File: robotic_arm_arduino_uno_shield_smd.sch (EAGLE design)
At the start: 39 parts, among them J1 (ID,OD)=(2.1,5.5)MM

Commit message: Adjusted some of the traces
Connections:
- net 5V: now also PLAY_SW.3, REC_SW.1; no longer PLAY_SW.1, REC_SW.3
- net D7: now also REC_SW.3; no longer REC_SW.1
- net D8: now also PLAY_SW.1; no longer PLAY_SW.3
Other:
- moved on the sheet: PLAY_SW, REC_SW
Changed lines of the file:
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@@
 <setting verticaltext="up"/>
 </settings>
-<grid distance="0.1" unitdist="inch" unit="inch" style="lines" multiple="1" display="no" altdistance="0.01" altunitdist="inch" altunit="inch"/>
+<grid distance="0.1" unitdist="inch" unit="inch" style="lines" multiple="1" display="yes" altdistance="0.01" altunitdist="inch" altunit="inch"/>
 <layers>
 <layer number="1" name="Top" color="4" fill="1" visible="no" active="no"/>
@@
 <instance part="SUPPLY5" gate="G$2" x="220.98" y="22.86"/>
 <instance part="SUPPLY6" gate="G$1" x="281.94" y="22.86"/>
-<instance part="REC_SW" gate="G$1" x="297.18" y="91.44" rot="R90"/>
-<instance part="PLAY_SW" gate="G$1" x="327.66" y="91.44" rot="R270"/>
+<instance part="REC_SW" gate="G$1" x="297.18" y="91.44" rot="R270"/>
+<instance part="PLAY_SW" gate="G$1" x="327.66" y="91.44" rot="R90"/>
 <instance part="R2" gate="G$1" x="327.66" y="73.66" rot="R90"/>
 <instance part="GND7" gate="GND" x="297.18" y="60.96"/>
@@
 <wire x1="335.28" y1="81.28" x2="327.66" y2="81.28" width="0.1524" layer="91"/>
 <label x="335.28" y="81.28" size="1.27" layer="95" ratio="10" xref="yes"/>
-<pinref part="PLAY_SW" gate="G$1" pin="3"/>
+<pinref part="PLAY_SW" gate="G$1" pin="1"/>
 <wire x1="327.66" y1="86.36" x2="327.66" y2="81.28" width="0.1524" layer="91"/>
 <junction x="327.66" y="81.28"/>
@@
 <segment>
 <pinref part="R1" gate="G$1" pin="2"/>
-<pinref part="REC_SW" gate="G$1" pin="1"/>
 <wire x1="297.18" y1="78.74" x2="297.18" y2="81.28" width="0.1524" layer="91"/>
+<wire x1="297.18" y1="81.28" x2="304.8" y2="81.28" width="0.1524" layer="91"/>
+<label x="304.8" y="81.28" size="1.27" layer="95" ratio="10" xref="yes"/>
+<pinref part="REC_SW" gate="G$1" pin="3"/>
 <wire x1="297.18" y1="81.28" x2="297.18" y2="86.36" width="0.1524" layer="91"/>
-<wire x1="297.18" y1="81.28" x2="304.8" y2="81.28" width="0.1524" layer="91"/>
 <junction x="297.18" y="81.28"/>
-<label x="304.8" y="81.28" size="1.27" layer="95" ratio="10" xref="yes"/>
 </segment>
 </net>
@@
 <net name="5V" class="0">
 <segment>
-<pinref part="REC_SW" gate="G$1" pin="3"/>
-<wire x1="297.18" y1="96.52" x2="297.18" y2="101.6" width="0.1524" layer="91"/>
-<pinref part="SUPPLY8" gate="5V" pin="5V"/>
-</segment>
-<segment>
 <wire x1="180.34" y1="-30.48" x2="190.5" y2="-30.48" width="0.1524" layer="91"/>
 <wire x1="190.5" y1="-30.48" x2="190.5" y2="-25.4" width="0.1524" layer="91"/>
@@
 </segment>
 <segment>
-<pinref part="PLAY_SW" gate="G$1" pin="1"/>
-<pinref part="SUPPLY9" gate="5V" pin="5V"/>
-<wire x1="327.66" y1="96.52" x2="327.66" y2="101.6" width="0.1524" layer="91"/>
-</segment>
-<segment>
 <pinref part="SUPPLY15" gate="5V" pin="5V"/>
 <wire x1="215.9" y1="99.06" x2="215.9" y2="91.44" width="0.1524" layer="91"/>
@@
 <wire x1="215.9" y1="91.44" x2="200.66" y2="91.44" width="0.1524" layer="91"/>
 </segment>
-</net>
+<segment>
+<pinref part="SUPPLY9" gate="5V" pin="5V"/>
+<pinref part="PLAY_SW" gate="G$1" pin="3"/>
+<wire x1="327.66" y1="101.6" x2="327.66" y2="96.52" width="0.1524" layer="91"/>
+</segment>
+<segment>
+<pinref part="REC_SW" gate="G$1" pin="1"/>
+<pinref part="SUPPLY8" gate="5V" pin="5V"/>
+<wire x1="297.18" y1="96.52" x2="297.18" y2="101.6" width="0.1524" layer="91"/>
+</segment>
+</net>

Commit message: Adjusted some of the traces
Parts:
- removed R5: 10KΩ, MrSwirlyEyes:RESISTORSMD-0805_1/8W_10K_5%
- added R0: 10KΩ, MrSwirlyEyes:RESISTORSMD-0805_1/8W_10K_5%
- BATT1, BATT2: value (none) -> 6V
- POT1, POT2, POT3, POT4: value (none) -> 22K
- renumbered C7 to C6, D1 to PWR_LED, S0 to PWR_SW
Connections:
- net GND: now also R0.1; no longer R5.1
- net N$1: now also R4.2; no longer R5.2
- net N$2: now also R3.2; no longer R4.2
- net N$4: now also R0.2; no longer R3.2
- net VCC_1: now also D5.A; no longer D4.A
- net VCC_2: now also D4.A; no longer D5.A
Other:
- moved on the sheet: R3, R4

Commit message: Final version.  Sending to fab
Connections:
- net N$3 renamed VBATT
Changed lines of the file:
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@@
 </segment>
 </net>
-<net name="N$3" class="0">
+<net name="VBATT" class="0">
 <segment>
 <wire x1="187.96" y1="175.26" x2="177.8" y2="175.26" width="0.1524" layer="91"/>

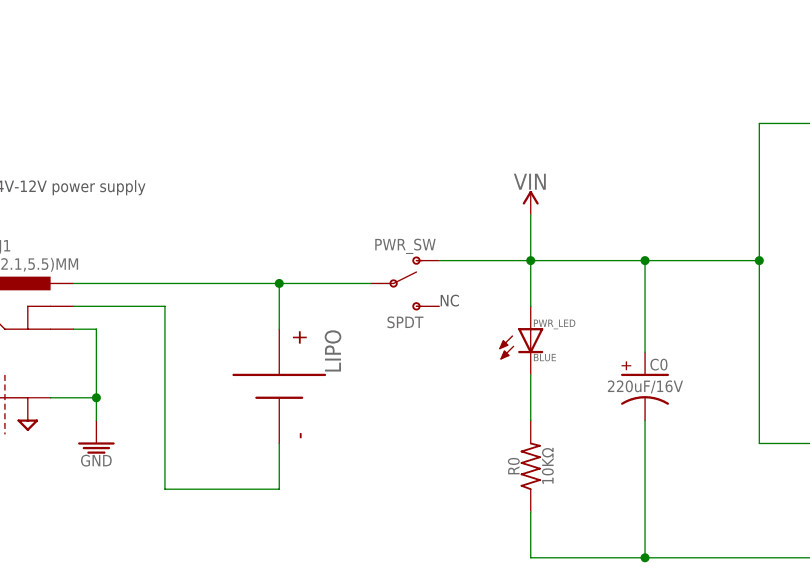
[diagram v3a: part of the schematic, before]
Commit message: Changed out switch.  Adjusted traces accordingly
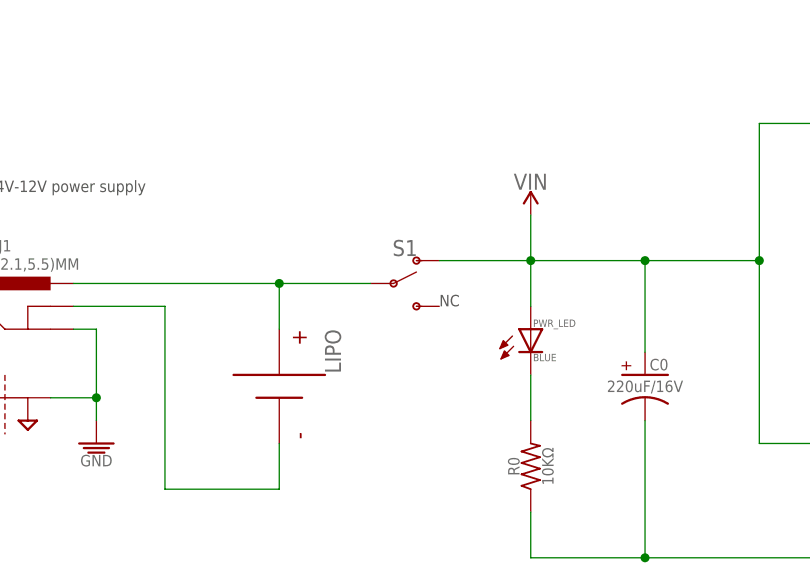
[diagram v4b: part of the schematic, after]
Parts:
- removed PWR_SW: SPDT, MrSwirlyEyes:SW_SPDT_RA_3A/28V/120VAC
- added S1: (no value), SparkFun-Switches:SWITCH-SPDT-PTH-11.6X4.0MM
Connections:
- net VBATT: now also S1.P; no longer PWR_SW.P
- net VIN: now also S1.O; no longer PWR_SW.S1
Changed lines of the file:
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@@
 <part name="C6" library="MrSwirlyEyes" deviceset="CAPACITOR_POLARIZED" device="_ALUM-ELECTROLYTIC_SMD_100UF-16V-20%" value="100UF/16V"/>
 <part name="LIPO" library="MrSwirlyEyes" deviceset="BATTERY" device=""/>
-<part name="PWR_SW" library="MrSwirlyEyes" deviceset="SW_SPDT_RA_3A/28V/120VAC" device="" value="SPDT"/>
 <part name="VREG1" library="MrSwirlyEyes" deviceset="VREG_LM340_LDO_1.5A-5V" device="" value="1.5A/5V"/>
 <part name="D4" library="MrSwirlyEyes" deviceset="DIODE_SMD_GP_1A-50V-SOD123F" device="" value="1A/50V"/>
@@
 <part name="NGND4" library="MrSwirlyEyes" deviceset="NGND" device=""/>
 <part name="NGND5" library="MrSwirlyEyes" deviceset="NGND" device=""/>
+<part name="S1" library="SparkFun-Switches" deviceset="SWITCH-SPDT" device="-PTH-11.6X4.0MM"/>
 </parts>
 <sheets>
@@
 <instance part="C6" gate="G$1" x="302.26" y="152.4"/>
 <instance part="LIPO" gate="G$1" x="177.8" y="162.56" rot="R270"/>
-<instance part="PWR_SW" gate="G$1" x="190.5" y="175.26"/>
 <instance part="VREG1" gate="G$1" x="264.16" y="193.04"/>
 <instance part="D4" gate="G$1" x="265.43" y="167.64" rot="R180"/>
@@
 <instance part="NGND4" gate="G$1" x="251.46" y="7.62"/>
 <instance part="NGND5" gate="G$1" x="281.94" y="7.62"/>
+<instance part="S1" gate="1" x="190.5" y="175.26"/>
 </instances>
 <busses>
@@
 <pinref part="PWR_LED" gate="G$1" pin="A"/>
 <wire x1="205.74" y1="172.72" x2="205.74" y2="177.8" width="0.1524" layer="91"/>
-<pinref part="PWR_SW" gate="G$1" pin="S1"/>
 <pinref part="VREG1" gate="G$1" pin="VI"/>
 <wire x1="254" y1="193.04" x2="251.46" y2="193.04" width="0.1524" layer="91"/>
@@
 <pinref part="D5" gate="G$1" pin="K"/>
 <wire x1="260.35" y1="203.2" x2="251.46" y2="203.2" width="0.1524" layer="91"/>
+<pinref part="S1" gate="1" pin="O"/>
 </segment>
 </net>
@@
 <junction x="177.8" y="175.26"/>
 <pinref part="LIPO" gate="G$1" pin="P"/>
-<pinref part="PWR_SW" gate="G$1" pin="P"/>
 <pinref part="J1" gate="G$1" pin="PWR"/>
-</segment>
-</net>
+<pinref part="S1" gate="1" pin="P"/>
+</segment>
+</net>

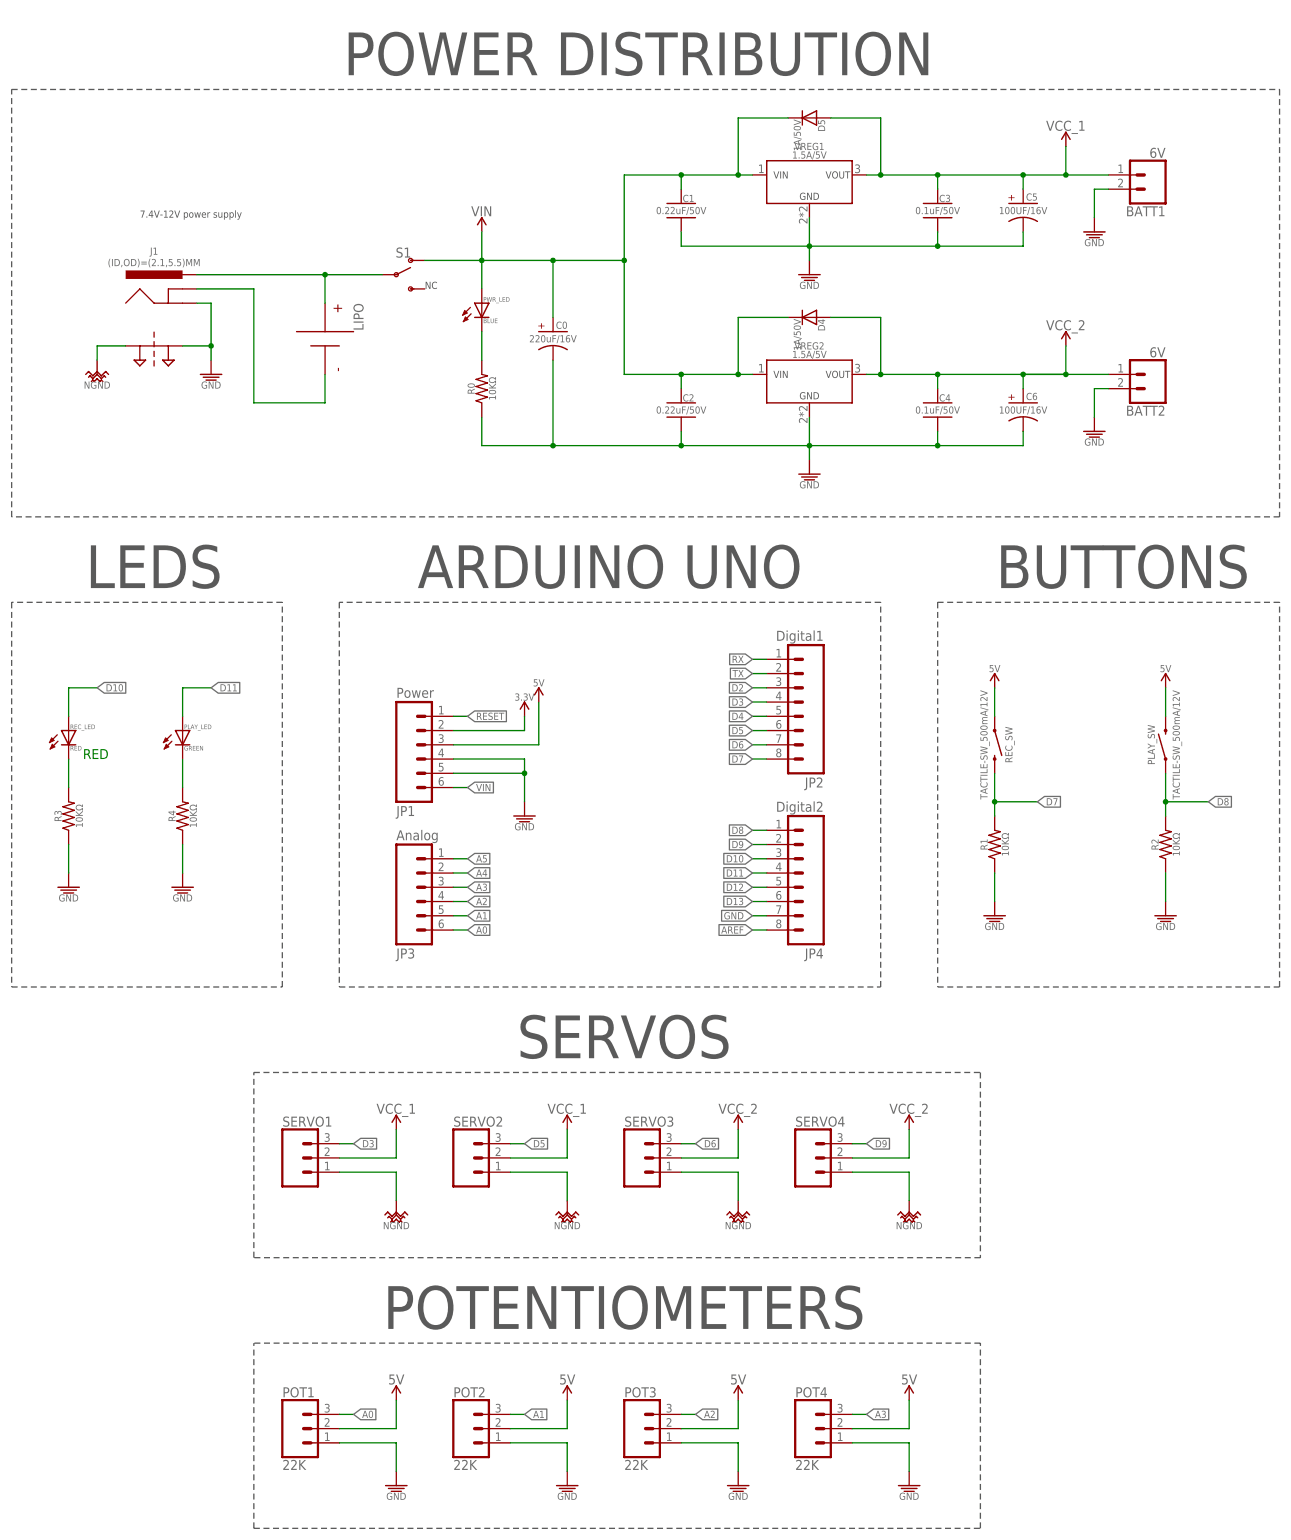
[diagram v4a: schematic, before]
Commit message: Rev 2.  Changed pad sizes of 805 SMD components.
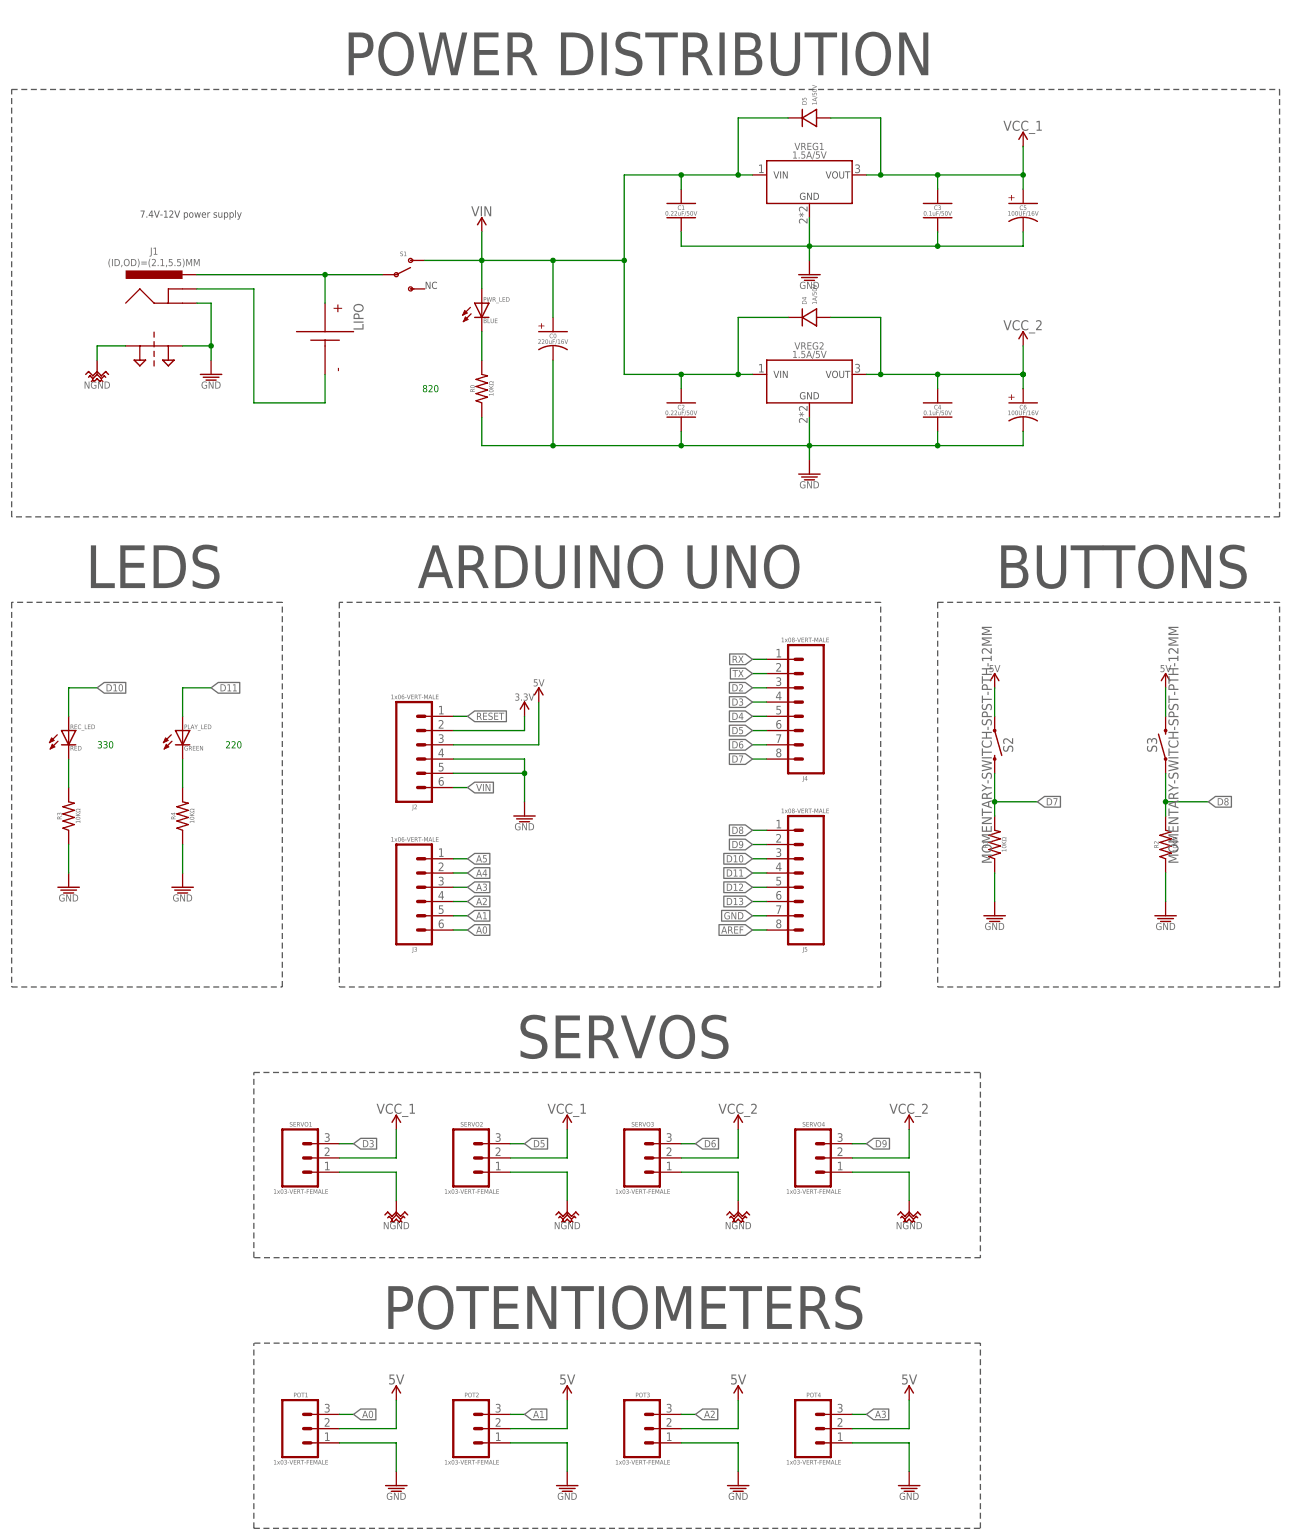
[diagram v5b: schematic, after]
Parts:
- removed BATT1, BATT2: 6V, SparkFun-Connectors:CONN_02
- removed JP1: Power, SparkFun:M06SIP
- removed JP2: Digital1, SparkFun:M08
- removed JP3: Analog, SparkFun:M06SIP
- removed JP4: Digital2, SparkFun:M08
- removed PLAY_SW, REC_SW: TACTILE-SW_500mA/12V, MrSwirlyEyes:SWITCH_MOMENTARY_SPST-NO_SMD_12V_50MA_5.2MM
- added J2, J3: 1x06-VERT-MALE, connectors:1X06VERT-MALE
- added J4, J5: 1x08-VERT-MALE, connectors:1X08VERT-MALE
- added S2, S3: MOMENTARY-SWITCH-SPST-PTH-12MM, SparkFun-Switches:MOMENTARY-SWITCH-SPST-PTH-12MM
- C0: device MrSwirlyEyes:CAPACITOR_POLARIZED_ALUM-ELECTROLYTIC_SMD_220UF-16V-20% -> MrSwirlyEyes:CAP_POLARIZED_ALUM-ELECTROLYTIC_SMD_220UF-16V-20%
- C1, C2: device MrSwirlyEyes:CAPACITOR_CERAMIC_SMD-805_0.22UF-50V-10% -> MrSwirlyEyes:CAP_CERAMIC_SMD-805_0.22UF-50V-10%
- C3, C4: device MrSwirlyEyes:CAPACITOR_CERAMIC_SMD-805_0.1UF-50V-10% -> MrSwirlyEyes:CAP_CERAMIC_SMD-805_0.1UF-50V-10%
- C5, C6: device MrSwirlyEyes:CAPACITOR_POLARIZED_ALUM-ELECTROLYTIC_SMD_100UF-16V-20% -> MrSwirlyEyes:CAP_POLARIZED_ALUM-ELECTROLYTIC_SMD_100UF-16V-20%
- D4, D5: device MrSwirlyEyes:DIODE_SMD_GP_1A-50V-SOD123F -> MrSwirlyEyes:DIODE_GEN-PURPSMD_GP_1A-50V-SOD123F
- LIPO: value BATTERY -> BATTERYPTH_HOLES; device MrSwirlyEyes:BATTERY -> MrSwirlyEyes:BATTERYPTH_HOLES
- PLAY_LED: device MrSwirlyEyes:LED-DISCRETE_SMD-805GREEN -> MrSwirlyEyes:LED_SMD-805_DISCRETE_GREEN
- POT1, POT2, POT3, POT4: value 22K -> 1x03-VERT-FEMALE; device SparkFun-Connectors:CONN_03 -> connectors:1X03VERT-FEMALE
- PWR_LED: device MrSwirlyEyes:LED-DISCRETE_SMD-805BLUE -> MrSwirlyEyes:LED_SMD-805_DISCRETE_BLUE
- REC_LED: device MrSwirlyEyes:LED-DISCRETE_SMD-805RED -> MrSwirlyEyes:LED_SMD-805_DISCRETE_RED
- S1: device SparkFun-Switches:SWITCH-SPDT-PTH-11.6X4.0MM -> MrSwirlyEyes:SWITCH_SPDT_SLIDE_RA_SMD_4V_300MA5A-28V_13L-7W
- SERVO1, SERVO2, SERVO3, SERVO4: value (none) -> 1x03-VERT-FEMALE; device SparkFun-Connectors:CONN_03 -> connectors:1X03VERT-FEMALE
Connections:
- net N$6 renamed -
- net VBATT renamed +
- net 3.3V: now also J2.2; no longer JP1.2
- net 5V: now also J2.3, S2.1, S3.2; no longer JP1.3, PLAY_SW.3, REC_SW.1
- net A0: now also J3.6; no longer JP3.6
- net A1: now also J3.5; no longer JP3.5
- net A2: now also J3.4; no longer JP3.4
- net A3: now also J3.3; no longer JP3.3
- net A4: now also J3.2; no longer JP3.2
- net A5: now also J3.1; no longer JP3.1
- net AREF: now also J5.8; no longer JP4.8
- net D10: now also J5.3; no longer JP4.3
- net D11: now also J5.4; no longer JP4.4
- net D12: now also J5.5; no longer JP4.5
- net D13: now also J5.6; no longer JP4.6
- net D2: now also J4.3; no longer JP2.3
- net D3: now also J4.4; no longer JP2.4
- net D4: now also J4.5; no longer JP2.5
- net D5: now also J4.6; no longer JP2.6
- net D6: now also J4.7; no longer JP2.7
- net D7: now also J4.8, S2.2; no longer JP2.8, REC_SW.3
- net D8: now also J5.1, S3.1; no longer JP4.1, PLAY_SW.1
- net D9: now also J5.2; no longer JP4.2
- net GND: now also J2.4, J2.5, J5.7; no longer BATT1.2, BATT2.2, JP1.4, JP1.5, JP4.7
- net RESET: now also J2.1; no longer JP1.1
- net RX: now also J4.1; no longer JP2.1
- net TX: now also J4.2; no longer JP2.2
- net VCC_1: no longer BATT1.1
- net VCC_2: no longer BATT2.1
- net VIN: now also J2.6, S1.S1; no longer JP1.6, S1.O
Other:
- note added: "220"
- note added: "330"
- note added: "820"
- note removed: "RED"

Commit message: Added switch object parameters for power switch and PLAY,RECORD buttons.  Added potentiometer from digikey to POT object.  Added Servo from Amazon to SERVO object MG90S
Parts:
- POT1, POT2, POT3, POT4: value 1x03-VERT-FEMALE -> 20KΩ; device connectors:1X03VERT-FEMALE -> MrSwirlyEyes:POTENTIOMETERNO-MARKINGS_VERT-FEMALE
- R3: value 10KΩ -> 2KΩ; device MrSwirlyEyes:RESISTORSMD-0805_1/8W_10K_5% -> MrSwirlyEyes:RESISTORSMD-0805_1/8W_2K_5%
- R4: value 10KΩ -> 1KΩ; device MrSwirlyEyes:RESISTORSMD-0805_1/8W_10K_5% -> MrSwirlyEyes:RESISTORSMD-0805_1/8W_1K_5%
- S1: value (none) -> 5A/28V; device MrSwirlyEyes:SWITCH_SPDT_SLIDE_RA_SMD_4V_300MA5A-28V_13L-7W -> MrSwirlyEyes:SWITCH_SPDT5A-28V_13L-7W
- S2, S3: value MOMENTARY-SWITCH-SPST-PTH-12MM -> (none); device SparkFun-Switches:MOMENTARY-SWITCH-SPST-PTH-12MM -> MrSwirlyEyes:SWITCH_MOMENTARY_SPSTSPST-PTH-L12-W12-H7.2
- SERVO1, SERVO2, SERVO3, SERVO4: value 1x03-VERT-FEMALE -> MG90S; device connectors:1X03VERT-FEMALE -> MrSwirlyEyes:SERVOMG90S_NO-MARKINGS
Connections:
- net 5V: now also POT1.CCW, POT2.CCW, POT3.CCW, POT4.CCW; no longer POT1.2, POT2.2, POT3.2, POT4.2
- net A0: now also POT1.S; no longer POT1.3
- net A1: now also POT2.S; no longer POT2.3
- net A2: now also POT3.S; no longer POT3.3
- net A3: now also POT4.S; no longer POT4.3
- net D3: now also SERVO1.SIG; no longer SERVO1.3
- net D5: now also SERVO2.SIG; no longer SERVO2.3
- net D6: now also SERVO3.SIG; no longer SERVO3.3
- net D9: now also SERVO4.SIG; no longer SERVO4.3
- net GND: now also POT1.CW, POT2.CW, POT3.CW, POT4.CW; no longer POT1.1, POT2.1, POT3.1, POT4.1
- net NGND: now also SERVO1.GND, SERVO2.GND, SERVO3.GND, SERVO4.GND; no longer SERVO1.1, SERVO2.1, SERVO3.1, SERVO4.1
- net VCC_1: now also SERVO1.VCC, SERVO2.VCC; no longer SERVO1.2, SERVO2.2
- net VCC_2: now also SERVO3.VCC, SERVO4.VCC; no longer SERVO3.2, SERVO4.2
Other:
- note removed: "220"
- note removed: "330"
- note removed: "820"
